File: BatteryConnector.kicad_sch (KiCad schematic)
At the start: 19 parts, among them J1 TopConn

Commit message: time flies when you're kicadding :(
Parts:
- C1: footprint Capacitor_SMD:C_0805_2012Metric_Pad1.18x1.45mm_HandSolder -> Capacitor_SMD:C_0805_2012Metric
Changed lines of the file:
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@@
       (effects (font (size 1.27 1.27)))
     )
-    (property "Footprint" "Capacitor_SMD:C_0805_2012Metric_Pad1.18x1.45mm_HandSolder" (at 130.175 89.2302 0)
+    (property "Footprint" "Capacitor_SMD:C_0805_2012Metric" (at 130.175 89.2302 0)
       (effects (font (size 1.27 1.27)) hide)
     )
@@
       (effects (font (size 1.27 1.27)))
     )
-    (property "Footprint" "Capacitor_SMD:C_0805_2012Metric_Pad1.18x1.45mm_HandSolder" (at 109.855 89.2302 0)
+    (property "Footprint" "Capacitor_SMD:C_0805_2012Metric" (at 109.855 89.2302 0)
       (effects (font (size 1.27 1.27)) hide)
     )
@@
       (effects (font (size 1.27 1.27)))
     )
-    (property "Footprint" "Capacitor_SMD:C_0805_2012Metric_Pad1.18x1.45mm_HandSolder" (at 79.375 89.2302 0)
+    (property "Footprint" "Capacitor_SMD:C_0805_2012Metric" (at 79.375 89.2302 0)
       (effects (font (size 1.27 1.27)) hide)
     )
@@
       (effects (font (size 1.27 1.27)))
     )
-    (property "Footprint" "Capacitor_SMD:C_0805_2012Metric_Pad1.18x1.45mm_HandSolder" (at 99.695 89.2302 0)
+    (property "Footprint" "Capacitor_SMD:C_0805_2012Metric" (at 99.695 89.2302 0)
       (effects (font (size 1.27 1.27)) hide)
     )
@@
       (effects (font (size 1.27 1.27)))
     )
-    (property "Footprint" "Capacitor_SMD:C_0805_2012Metric_Pad1.18x1.45mm_HandSolder" (at 89.535 89.2302 0)
+    (property "Footprint" "Capacitor_SMD:C_0805_2012Metric" (at 89.535 89.2302 0)
       (effects (font (size 1.27 1.27)) hide)
     )
@@
       (effects (font (size 1.27 1.27)))
     )
-    (property "Footprint" "Capacitor_SMD:C_0805_2012Metric_Pad1.18x1.45mm_HandSolder" (at 120.015 89.2302 0)
-      (effects (font (size 1.27 1.27)) hide)
-    )
+    (property "Footprint" "Capacitor_SMD:C_0805_2012Metric" (at 120.015 89.2302 0)
+      (effects (font (size 1.27 1.27)) hide)
+    )

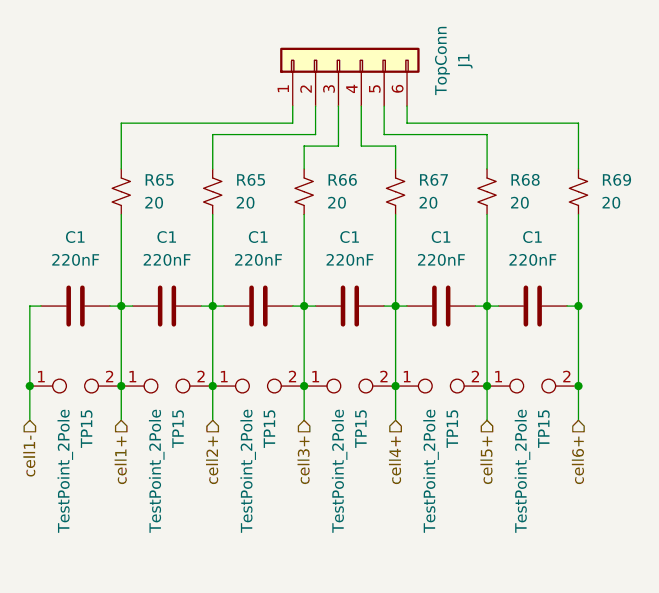
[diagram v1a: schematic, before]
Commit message: new ADC layout
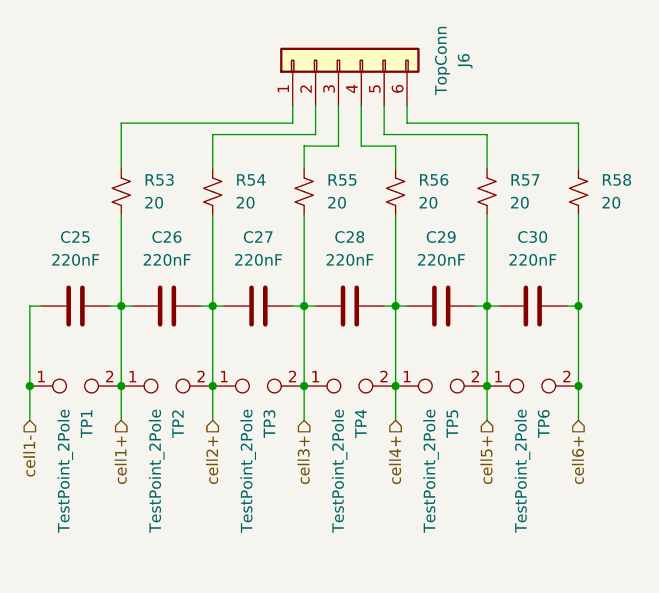
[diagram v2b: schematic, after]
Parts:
- renumbered C1 to C25, C1 to C26, C1 to C27, C1 to C28, C1 to C29, C1 to C30, J1 to J6, R65 to R53, R65 to R54, R66 to R55, R67 to R56, R68 to R57, R69 to R58, TP15 to TP1, TP15 to TP2, TP15 to TP3, TP15 to TP4, TP15 to TP5, TP15 to TP6
